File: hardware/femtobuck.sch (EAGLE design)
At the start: 11 parts

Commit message: Incorporate changes from review
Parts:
- added JP2: M02PTH, SparkFun-Connectors:M02PTH
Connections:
- net OUT+: now also JP2.1
- net OUT-: now also JP2.2
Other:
- note added: "Mike Hord"
- note removed: "Ethan Zonca/Mike Hord"
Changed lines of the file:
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@@
 <part name="GND1" library="SparkFun" deviceset="GND" device=""/>
 <part name="LOGO2" library="SparkFun-Aesthetics" deviceset="SFE_LOGO_NAME_FLAME" device=".1_INCH" value="SFE_LOGO_NAME_FLAME.1_INCH"/>
+<part name="JP2" library="SparkFun-Connectors" deviceset="M02" device="PTH"/>
 </parts>
 <sheets>
@@
 </text>
 <text x="238.506" y="6.604" size="3.81" layer="91">01</text>
-<text x="153.924" y="6.35" size="3.81" layer="91">Ethan Zonca/Mike Hord</text>
+<text x="153.924" y="6.35" size="3.81" layer="91">Mike Hord</text>
 </plain>
 <instances>
@@
 <instance part="GND1" gate="1" x="190.5" y="119.38"/>
 <instance part="LOGO2" gate="G$1" x="88.9" y="2.54"/>
+<instance part="JP2" gate="G$1" x="144.78" y="99.06" rot="R180"/>
 </instances>
 <busses>
@@
 <junction x="127" y="104.14"/>
 <pinref part="L1" gate="G$1" pin="2"/>
-<wire x1="134.62" y1="104.14" x2="127" y2="104.14" width="0.1524" layer="91"/>
-<wire x1="134.62" y1="104.14" x2="134.62" y2="109.22" width="0.1524" layer="91"/>
+<wire x1="132.08" y1="104.14" x2="127" y2="104.14" width="0.1524" layer="91"/>
+<wire x1="132.08" y1="104.14" x2="132.08" y2="109.22" width="0.1524" layer="91"/>
 <pinref part="CH1" gate="G$1" pin="1"/>
-<wire x1="134.62" y1="109.22" x2="137.16" y2="109.22" width="0.1524" layer="91"/>
+<wire x1="132.08" y1="109.22" x2="137.16" y2="109.22" width="0.1524" layer="91"/>
+<pinref part="JP2" gate="G$1" pin="2"/>
+<wire x1="137.16" y1="96.52" x2="132.08" y2="96.52" width="0.1524" layer="91"/>
+<wire x1="132.08" y1="96.52" x2="132.08" y2="104.14" width="0.1524" layer="91"/>
+<junction x="132.08" y="104.14"/>
 </segment>
 </net>
@@
 <wire x1="129.54" y1="119.38" x2="129.54" y2="116.84" width="0.1524" layer="91"/>
 <junction x="129.54" y="116.84"/>
+<wire x1="134.62" y1="111.76" x2="134.62" y2="99.06" width="0.1524" layer="91"/>
+<junction x="134.62" y="111.76"/>
+<pinref part="JP2" gate="G$1" pin="1"/>
+<wire x1="134.62" y1="99.06" x2="137.16" y2="99.06" width="0.1524" layer="91"/>
 </segment>
 </net>

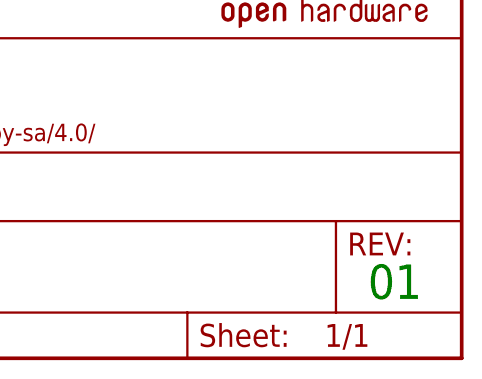
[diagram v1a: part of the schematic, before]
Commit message: Small updates for production
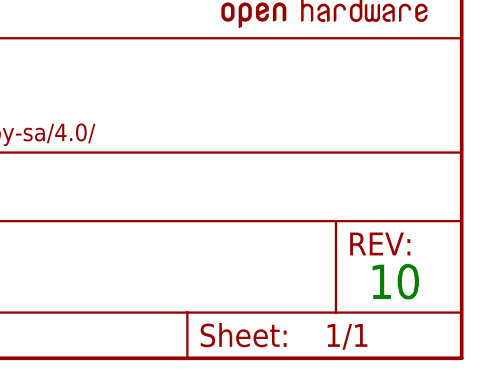
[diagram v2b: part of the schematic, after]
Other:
- note added: "10"
- note removed: "01"
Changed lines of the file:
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@@
    V_thd = 0.1
 </text>
-<text x="238.506" y="6.604" size="3.81" layer="91">01</text>
+<text x="238.506" y="6.604" size="3.81" layer="91">10</text>
 <text x="153.924" y="6.35" size="3.81" layer="91">Mike Hord</text>
 </plain>

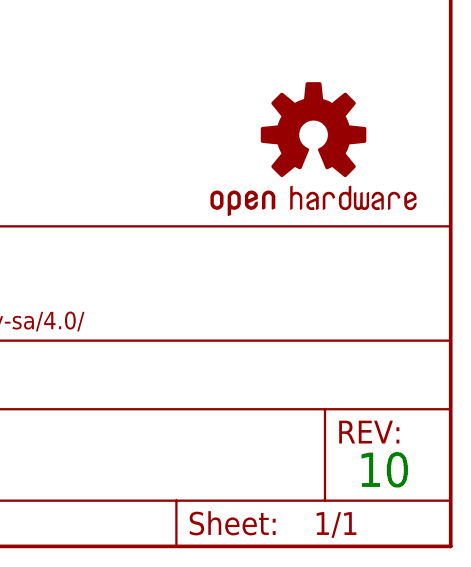
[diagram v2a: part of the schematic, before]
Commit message: added board fiducials
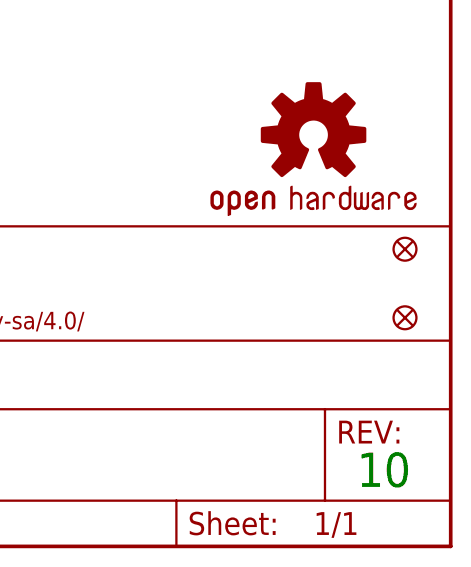
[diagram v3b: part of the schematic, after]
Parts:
- added FID1, FID2: FIDUCIAL1X2, SparkFun-Aesthetics:FIDUCIAL1X2
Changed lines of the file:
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@@
 <part name="LOGO2" library="SparkFun-Aesthetics" deviceset="SFE_LOGO_NAME_FLAME" device=".1_INCH" value="SFE_LOGO_NAME_FLAME.1_INCH"/>
 <part name="JP2" library="SparkFun-Connectors" deviceset="M02" device="PTH"/>
+<part name="FID1" library="SparkFun-Aesthetics" deviceset="FIDUCIAL" device="1X2"/>
+<part name="FID2" library="SparkFun-Aesthetics" deviceset="FIDUCIAL" device="1X2"/>
 </parts>
 <sheets>
@@
 <instance part="LOGO2" gate="G$1" x="88.9" y="2.54"/>
 <instance part="JP2" gate="G$1" x="144.78" y="99.06" rot="R180"/>
+<instance part="FID1" gate="G$1" x="243.84" y="33.02"/>
+<instance part="FID2" gate="G$1" x="243.84" y="25.4"/>
 </instances>
 <busses>

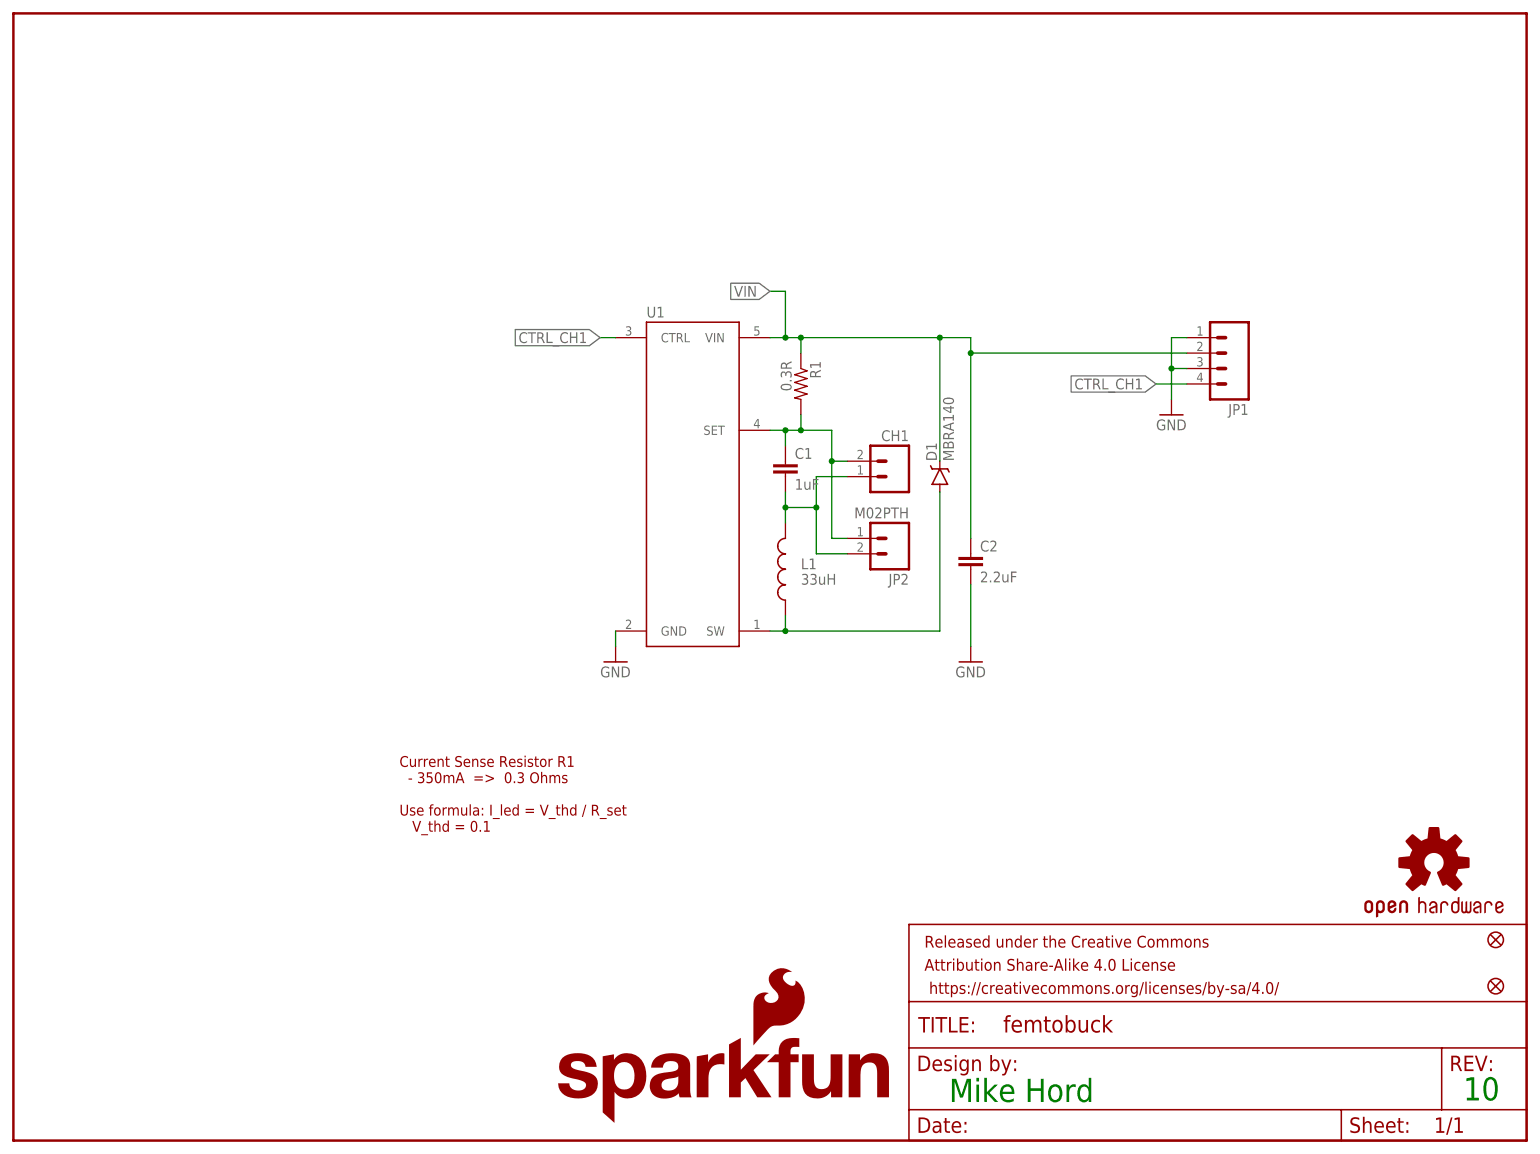
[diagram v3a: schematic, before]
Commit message: Added 2nd sense resistor, jumper
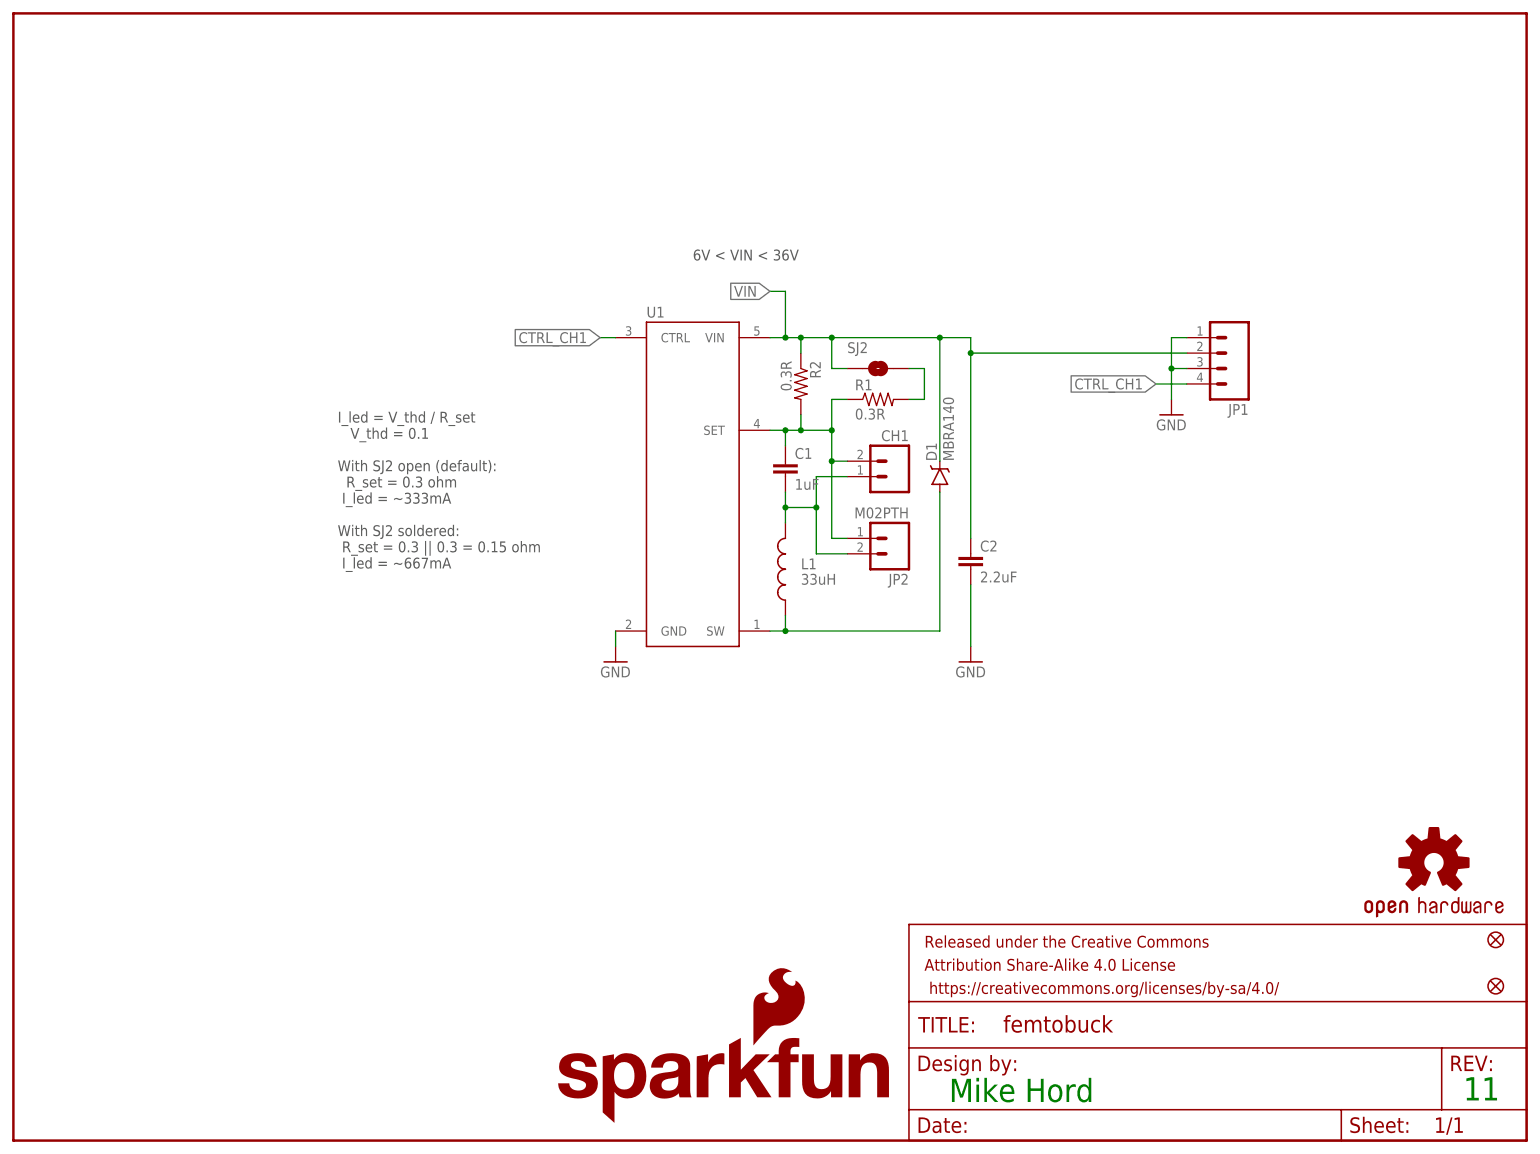
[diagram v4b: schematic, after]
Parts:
- added R2: 0.3R, SparkFun-Resistors:0.3OHM-1/8W-1%(0805)
- added SJ2: NO Jumper, SparkFun-Passives:JUMPER-PAD-2-NO
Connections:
- new net N$1: R1.2, SJ2.2
- net OUT+: now also R1.1, R2.2; no longer R1.2
- net VIN: now also R2.1, SJ2.1; no longer R1.1
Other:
- note added: "11"
- note added: "6V < VIN < 36V"
- note added: "I_led = V_thd / R_set V_thd = 0.1 With SJ2 open (default): R_set = 0.3 ohm I_led = ~333mA With SJ2 soldered: R_set = 0.3 || 0.3 = 0.15 ohm I_led = ~667mA"
- note removed: "10"
- note removed: "Current Sense Resistor R1 - 350mA => 0.3 Ohms Use formula: I_led = V_thd / R_set V_thd = 0.1"
- moved on the sheet: R1
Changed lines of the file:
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@@
 <?xml version="1.0" encoding="utf-8"?>
 <!DOCTYPE eagle SYSTEM "eagle.dtd">
-<eagle version="6.5.0">
+<eagle version="7.3.0">
 <drawing>
 <settings>
@@
 <layer number="254" name="cooling" color="7" fill="1" visible="yes" active="yes"/>
 </layers>
-<schematic xreflabel="%F%N/%S.%C%R" xrefpart="/%S.%C%R">
+<schematic xreflabel="%F%N/%S" xrefpart="1_/%S.%C%R">
 <attributes>
 </attributes>
@@
 <part name="FID1" library="SparkFun-Aesthetics" deviceset="FIDUCIAL" device="1X2"/>
 <part name="FID2" library="SparkFun-Aesthetics" deviceset="FIDUCIAL" device="1X2"/>
+<part name="R2" library="SparkFun-Resistors" deviceset="0.3OHM-1/8W-1%(0805)" device="" value="0.3R"/>
+<part name="SJ2" library="SparkFun-Passives" deviceset="JUMPER-PAD-2-NO" device="" value="NO Jumper"/>
 </parts>
 <sheets>
 <sheet>
 <plain>
-<text x="63.5" y="50.8" size="1.778" layer="94">Current Sense Resistor R1
-  - 350mA  =&gt;  0.3 Ohms
-Use formula: I_led = V_thd / R_set
+<text x="53.34" y="91.44" size="1.778" layer="97">I_led = V_thd / R_set
    V_thd = 0.1
-</text>
-<text x="238.506" y="6.604" size="3.81" layer="91">10</text>
+With SJ2 open (default):
+  R_set = 0.3 ohm
+ I_led = ~333mA
+With SJ2 soldered:
+ R_set = 0.3 || 0.3 = 0.15 ohm
+ I_led = ~667mA
+ </text>
+<text x="238.506" y="6.604" size="3.81" layer="91">11</text>
 <text x="153.924" y="6.35" size="3.81" layer="91">Mike Hord</text>
+<text x="111.76" y="144.78" size="1.778" layer="97">6V &lt; VIN &lt; 36V</text>
 </plain>
 <instances>
 <instance part="U1" gate="G$1" x="111.76" y="114.3"/>
-<instance part="R1" gate="G$1" x="129.54" y="124.46" rot="R270"/>
+<instance part="R1" gate="G$1" x="142.24" y="121.92"/>
 <instance part="C1" gate="G$1" x="127" y="109.22"/>
 <instance part="C2" gate="G$1" x="157.48" y="93.98"/>
@@
 <instance part="FID1" gate="G$1" x="243.84" y="33.02"/>
 <instance part="FID2" gate="G$1" x="243.84" y="25.4"/>
+<instance part="R2" gate="G$1" x="129.54" y="124.46" rot="R270"/>
+<instance part="SJ2" gate="G$1" x="142.24" y="127" smashed="yes">
+<attribute name="NAME" x="137.16" y="129.54" size="1.778" layer="95"/>
+</instance>
 </instances>
 <busses>
@@
 <wire x1="157.48" y1="132.08" x2="157.48" y2="129.54" width="0.1524" layer="91"/>
 <wire x1="157.48" y1="129.54" x2="157.48" y2="99.06" width="0.1524" layer="91"/>
+<junction x="127" y="132.08"/>
 <wire x1="127" y1="132.08" x2="129.54" y2="132.08" width="0.1524" layer="91"/>
-<junction x="127" y="132.08"/>
-<wire x1="129.54" y1="132.08" x2="152.4" y2="132.08" width="0.1524" layer="91"/>
+<wire x1="129.54" y1="132.08" x2="134.62" y2="132.08" width="0.1524" layer="91"/>
+<wire x1="134.62" y1="132.08" x2="152.4" y2="132.08" width="0.1524" layer="91"/>
 <wire x1="127" y1="132.08" x2="127" y2="139.7" width="0.1524" layer="91"/>
 <wire x1="127" y1="139.7" x2="124.46" y2="139.7" width="0.1524" layer="91"/>
@@
 <wire x1="193.04" y1="129.54" x2="157.48" y2="129.54" width="0.1524" layer="91"/>
 <junction x="157.48" y="129.54"/>
-<pinref part="R1" gate="G$1" pin="1"/>
+<pinref part="R2" gate="G$1" pin="1"/>
 <wire x1="129.54" y1="129.54" x2="129.54" y2="132.08" width="0.1524" layer="91"/>
 <junction x="129.54" y="132.08"/>
+<pinref part="SJ2" gate="G$1" pin="1"/>
+<wire x1="137.16" y1="127" x2="134.62" y2="127" width="0.1524" layer="91"/>
+<wire x1="134.62" y1="127" x2="134.62" y2="132.08" width="0.1524" layer="91"/>
+<junction x="134.62" y="132.08"/>
 </segment>
 </net>
@@
 <pinref part="CH1" gate="G$1" pin="2"/>
 <wire x1="134.62" y1="111.76" x2="137.16" y2="111.76" width="0.1524" layer="91"/>
-<pinref part="R1" gate="G$1" pin="2"/>
-<wire x1="129.54" y1="119.38" x2="129.54" y2="116.84" width="0.1524" layer="91"/>
-<junction x="129.54" y="116.84"/>
 <wire x1="134.62" y1="111.76" x2="134.62" y2="99.06" width="0.1524" layer="91"/>
 <junction x="134.62" y="111.76"/>
 <pinref part="JP2" gate="G$1" pin="1"/>
 <wire x1="134.62" y1="99.06" x2="137.16" y2="99.06" width="0.1524" layer="91"/>
+<pinref part="R2" gate="G$1" pin="2"/>
+<wire x1="129.54" y1="119.38" x2="129.54" y2="116.84" width="0.1524" layer="91"/>
+<junction x="129.54" y="116.84"/>
+<wire x1="134.62" y1="116.84" x2="134.62" y2="121.92" width="0.1524" layer="91"/>
+<junction x="134.62" y="116.84"/>
+<pinref part="R1" gate="G$1" pin="1"/>
+<wire x1="134.62" y1="121.92" x2="137.16" y2="121.92" width="0.1524" layer="91"/>
 </segment>
 </net>
@@
 </segment>
 </net>
+<net name="N$1" class="0">
+<segment>
+<pinref part="R1" gate="G$1" pin="2"/>
+<wire x1="147.32" y1="121.92" x2="149.86" y2="121.92" width="0.1524" layer="91"/>
+<wire x1="149.86" y1="121.92" x2="149.86" y2="127" width="0.1524" layer="91"/>
+<pinref part="SJ2" gate="G$1" pin="2"/>
+<wire x1="149.86" y1="127" x2="147.32" y2="127" width="0.1524" layer="91"/>
+</segment>
+</net>

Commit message: Fixed changes from QC
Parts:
- U1: value (none) -> AL8805
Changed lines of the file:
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@@
 </classes>
 <parts>
-<part name="U1" library="SparkFun-PowerIC" deviceset="AL8805" device=""/>
+<part name="U1" library="SparkFun-PowerIC" deviceset="AL8805" device="" value="AL8805"/>
 <part name="R1" library="SparkFun-Resistors" deviceset="0.3OHM-1/8W-1%(0805)" device="" value="0.3R"/>
 <part name="C1" library="SparkFun-Capacitors" deviceset="1.0UF50V10%(1206)" device="" value="1uF"/>

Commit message: Chg to 12, inc. line wid on logos
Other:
- note added: "12"
- note removed: "11"
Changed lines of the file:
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@@
 <layer number="54" name="bGND_GNDA" color="1" fill="9" visible="no" active="no"/>
 <layer number="56" name="wert" color="7" fill="1" visible="no" active="no"/>
+<layer number="57" name="tCAD" color="7" fill="1" visible="no" active="no"/>
+<layer number="59" name="tCarbon" color="7" fill="1" visible="no" active="no"/>
+<layer number="60" name="bCarbon" color="7" fill="1" visible="no" active="no"/>
+<layer number="90" name="Modules" color="5" fill="1" visible="yes" active="yes"/>
 <layer number="91" name="Nets" color="2" fill="1" visible="yes" active="yes"/>
 <layer number="92" name="Busses" color="1" fill="1" visible="yes" active="yes"/>
@@
 <layer number="97" name="Info" color="7" fill="1" visible="yes" active="yes"/>
 <layer number="98" name="Guide" color="6" fill="1" visible="yes" active="yes"/>
+<layer number="99" name="SpiceOrder" color="7" fill="1" visible="no" active="no"/>
 <layer number="100" name="Muster" color="7" fill="1" visible="no" active="no"/>
 <layer number="101" name="Patch_Top" color="12" fill="4" visible="yes" active="yes"/>
@@
 <layer number="127" name="_tValues" color="7" fill="1" visible="yes" active="yes"/>
 <layer number="128" name="_bValues" color="7" fill="1" visible="yes" active="yes"/>
+<layer number="129" name="Mask" color="7" fill="1" visible="yes" active="yes"/>
 <layer number="131" name="prix" color="7" fill="1" visible="yes" active="yes"/>
 <layer number="132" name="test" color="7" fill="1" visible="yes" active="yes"/>
 <layer number="144" name="Drill_legend" color="7" fill="1" visible="no" active="yes"/>
+<layer number="150" name="Notes" color="7" fill="1" visible="yes" active="yes"/>
 <layer number="151" name="HeatSink" color="7" fill="1" visible="yes" active="yes"/>
 <layer number="152" name="_bDocu" color="7" fill="1" visible="yes" active="yes"/>
+<layer number="153" name="FabDoc1" color="7" fill="1" visible="yes" active="yes"/>
+<layer number="154" name="FabDoc2" color="7" fill="1" visible="yes" active="yes"/>
+<layer number="155" name="FabDoc3" color="7" fill="1" visible="yes" active="yes"/>
 <layer number="199" name="Contour" color="7" fill="1" visible="no" active="yes"/>
 <layer number="200" name="200bmp" color="1" fill="10" visible="yes" active="yes"/>
@@
 <layer number="223" name="223bmp" color="24" fill="1" visible="no" active="no"/>
 <layer number="224" name="224bmp" color="25" fill="1" visible="no" active="no"/>
+<layer number="225" name="225bmp" color="7" fill="1" visible="yes" active="yes"/>
+<layer number="226" name="226bmp" color="7" fill="1" visible="yes" active="yes"/>
+<layer number="227" name="227bmp" color="7" fill="1" visible="yes" active="yes"/>
+<layer number="228" name="228bmp" color="7" fill="1" visible="yes" active="yes"/>
+<layer number="229" name="229bmp" color="7" fill="1" visible="yes" active="yes"/>
+<layer number="230" name="230bmp" color="7" fill="1" visible="yes" active="yes"/>
+<layer number="231" name="231bmp" color="7" fill="1" visible="yes" active="yes"/>
 <layer number="248" name="Housing" color="7" fill="1" visible="yes" active="yes"/>
 <layer number="249" name="Edge" color="7" fill="1" visible="yes" active="yes"/>
@@
 <layer number="251" name="SMDround" color="12" fill="11" visible="no" active="no"/>
 <layer number="254" name="cooling" color="7" fill="1" visible="yes" active="yes"/>
+<layer number="255" name="routoute" color="7" fill="1" visible="yes" active="yes"/>
 </layers>
-<schematic xreflabel="%F%N/%S" xrefpart="1_/%S.%C%R">
+<schematic xreflabel="%F%N/%S" xrefpart="/%S.%C%R">
 <attributes>
 </attributes>
@@
  I_led = ~667mA
  </text>
-<text x="238.506" y="6.604" size="3.81" layer="91">11</text>
+<text x="238.506" y="6.604" size="3.81" layer="91">12</text>
 <text x="153.924" y="6.35" size="3.81" layer="91">Mike Hord</text>
 <text x="111.76" y="144.78" size="1.778" layer="97">6V &lt; VIN &lt; 36V</text>
@@
 <instance part="LOGO1" gate="G$1" x="233.68" y="45.72"/>
 <instance part="FRAME1" gate="G$1" x="0" y="0"/>
-<instance part="FRAME1" gate="G$2" x="147.32" y="0"/>
+<instance part="FRAME1" gate="V" x="147.32" y="0"/>
 <instance part="JP1" gate="G$1" x="198.12" y="129.54" rot="R180"/>
 <instance part="GND1" gate="1" x="190.5" y="119.38"/>
